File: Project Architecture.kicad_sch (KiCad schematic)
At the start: 4 parts

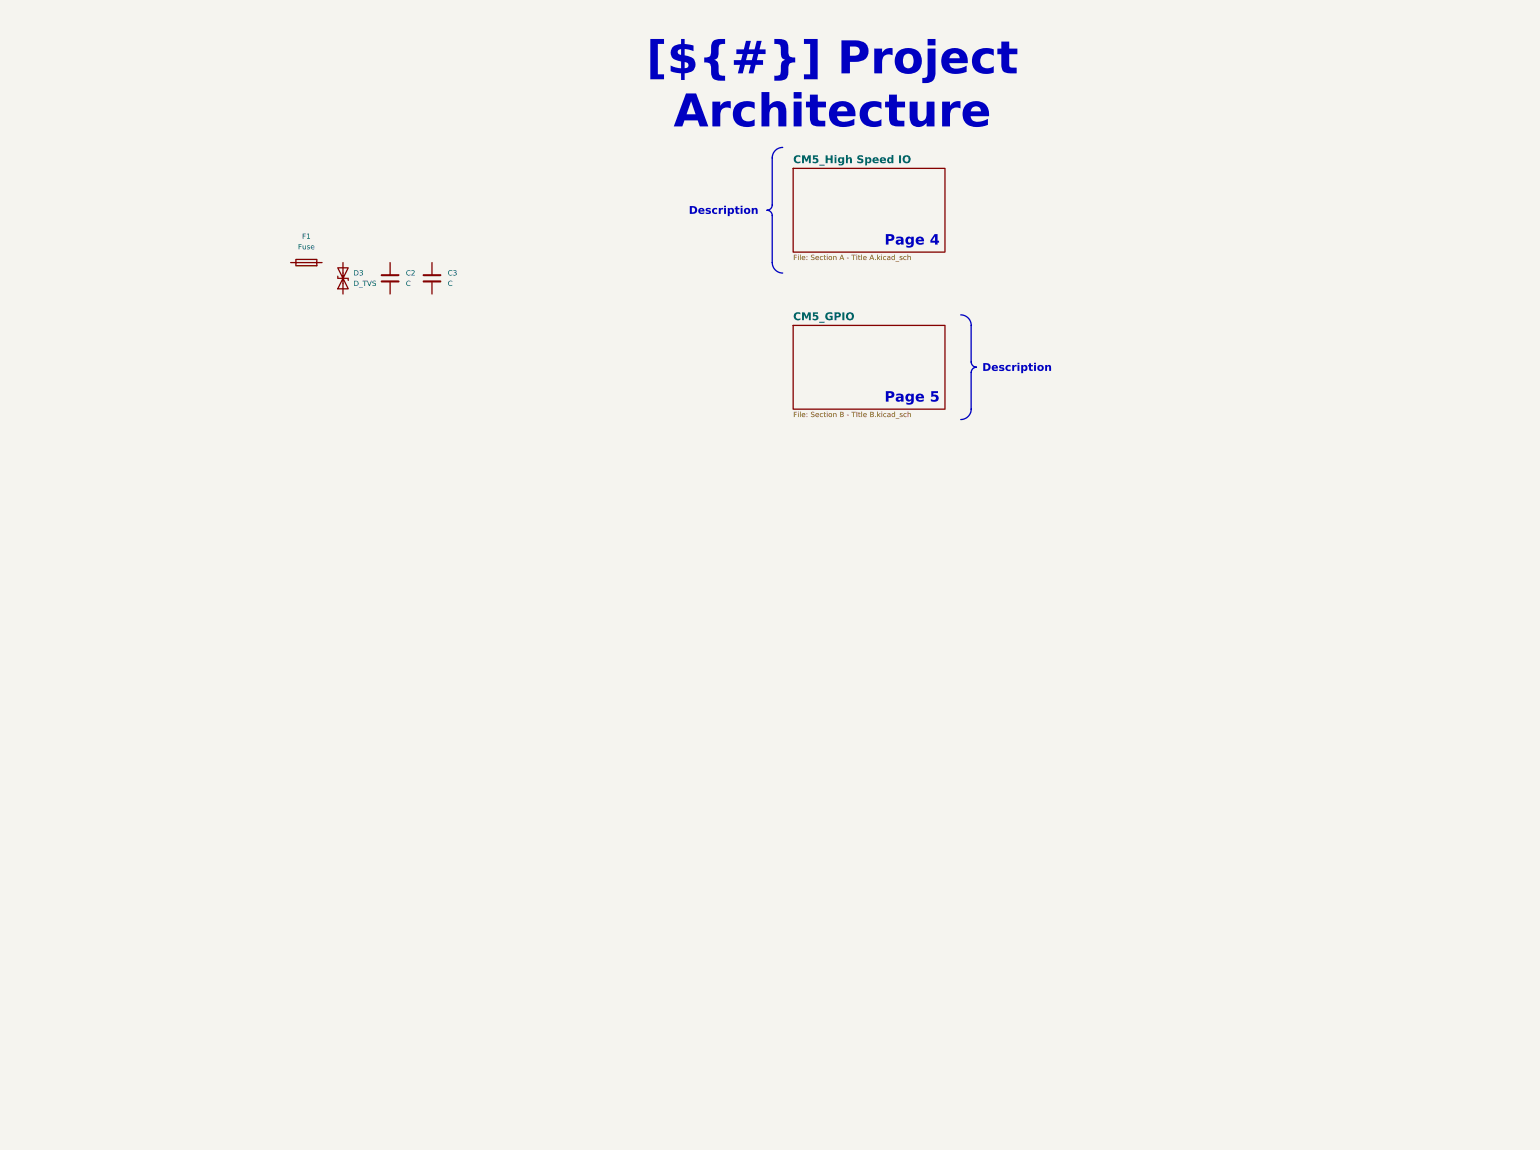
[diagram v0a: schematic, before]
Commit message: Progress in power input and sata power option
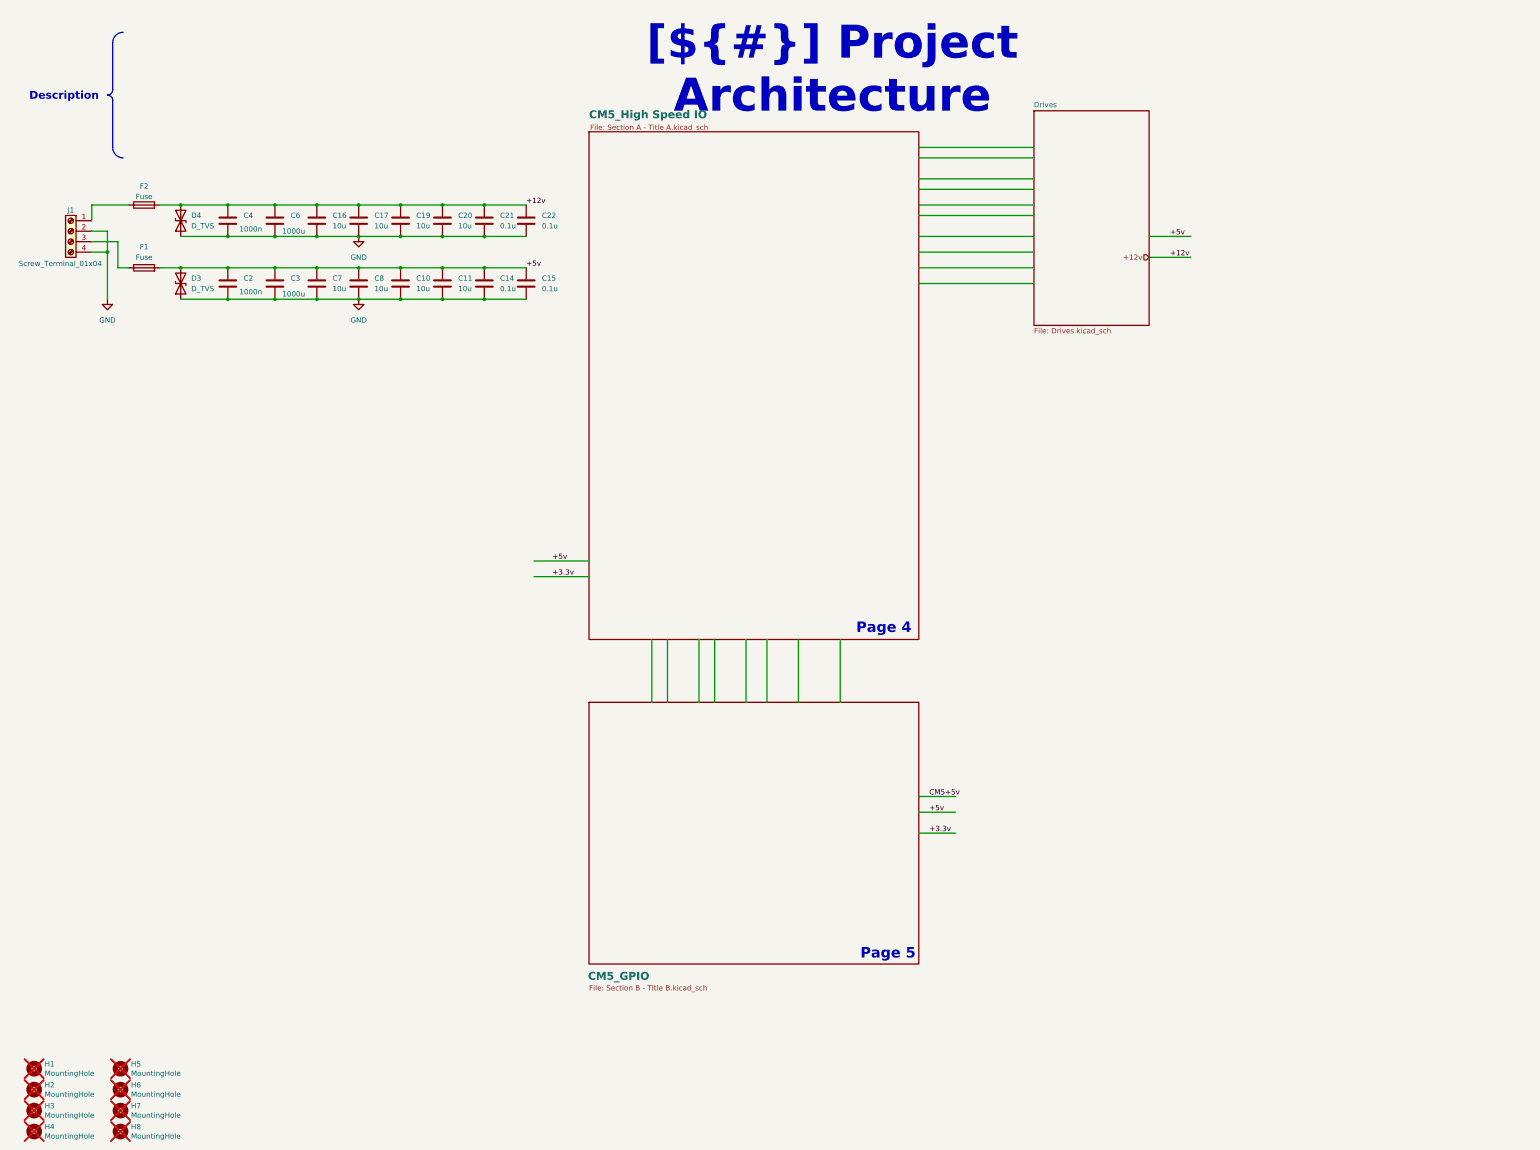
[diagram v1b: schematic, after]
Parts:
- added C10, C11, C16, C17, C19, C20, C7, C8: 10u, symbol Device:C
- added C14, C15, C21, C22: 0.1u, symbol Device:C
- added C4: 1000n, symbol Device:C
- added C6: 1000u, symbol Device:C
- added D4: D_TVS, symbol Device:D_TVS
- added F2: Fuse, symbol Device:Fuse
- added H1, H2, H3, H4, H5, H6, H7, H8: MountingHole, CM5IO:MountingHole_2.7mm_M2.5_DIN965, symbol Mechanical:MountingHole
- added J1: Screw_Terminal_01x04, symbol Connector:Screw_Terminal_01x04
- C2: value C -> 1000n
- C3: value C -> 1000u
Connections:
- net at F1.1: now also J1.3 (Pin_3)
- net +5v: now reaches F1.2
- net +5v: now also C2.1, C3.1, D3.2 (A2), C10.1, C11.1, C14.1, C15.1, C7.1, C8.1
- net GND: now reaches C2.2
- net GND: now also C3.2, D3.1 (A1), C10.2, C11.2, C14.2, C15.2, C16.2, C17.2, C19.2, C20.2, C21.2, C22.2, C4.2, C6.2, C7.2, C8.2, D4.1 (A1), J1.2 (Pin_2), J1.4 (Pin_4)
- new net: F2.1, J1.1 (Pin_1)
- new net +12v: C16.1, C17.1, C19.1, C20.1, C21.1, C22.1, C4.1, C6.1, D4.2 (A2), F2.2
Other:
- added sheet Drives (Drives.kicad_sch)
- moved on the sheet: C2, C3, D3, F1

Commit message: Voltage calcs
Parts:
- renumbered C4 to C1, C20 to C11, C11 to C12, C21 to C13, C22 to C15, C15 to C16, C6 to C3, C3 to C4, C16 to C5, C7 to C6, C17 to C7, C19 to C9, D4 to D1, D3 to D2, F2 to F1, F1 to F2
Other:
- added sheet Sata Drives (Sata_Drives.kicad_sch)
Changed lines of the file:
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@@
 	(wire
 		(pts
+			(xy 231.14 78.74) (xy 259.08 78.74)
+		)
+		(stroke
+			(width 0)
+			(type solid)
+		)
+	)
+	(wire
+		(pts
 			(xy 125.73 63.5) (xy 135.89 63.5)
 		)
@@
 	(wire
 		(pts
+			(xy 231.14 82.55) (xy 259.08 82.55)
+		)
+		(stroke
+			(width 0)
+			(type solid)
+		)
+	)
+	(wire
+		(pts
 			(xy 170.18 161.29) (xy 170.18 176.53)
 		)
@@
 		(on_board yes)
 		(dnp no)
-		(property "Reference" "F2"
+		(property "Reference" "F1"
 			(at 43.18 51.308 90)
 			(effects
@@
 			(project "CM5 Nas"
 				(path "/0650c7a8-acba-429c-9f8e-eec0baf0bc1c/fede4c36-00cc-4d3d-b71c-5243ba232202"
-					(reference "F2")
+					(reference "F1")
 					(unit 1)
 				)
@@
 		(dnp no)
 		(fields_autoplaced yes)
-		(property "Reference" "C22"
+		(property "Reference" "C15"
 			(at 139.7 58.4199 0)
 			(effects
@@
 			(project "CM5 Nas"
 				(path "/0650c7a8-acba-429c-9f8e-eec0baf0bc1c/fede4c36-00cc-4d3d-b71c-5243ba232202"
-					(reference "C22")
+					(reference "C15")
 					(unit 1)
 				)
@@
 		(on_board yes)
 		(dnp no)
-		(property "Reference" "C4"
+		(property "Reference" "C1"
 			(at 67.31 58.4199 0)
 			(effects
@@
 			(project "CM5 Nas"
 				(path "/0650c7a8-acba-429c-9f8e-eec0baf0bc1c/fede4c36-00cc-4d3d-b71c-5243ba232202"
-					(reference "C4")
+					(reference "C1")
 					(unit 1)
 				)
@@
 		(dnp no)
 		(fields_autoplaced yes)
-		(property "Reference" "#PWR03"
+		(property "Reference" "#PWR02"
 			(at 95.25 69.85 0)
 			(effects
@@
 			(project "CM5 Nas"
 				(path "/0650c7a8-acba-429c-9f8e-eec0baf0bc1c/fede4c36-00cc-4d3d-b71c-5243ba232202"
-					(reference "#PWR03")
+					(reference "#PWR02")
 					(unit 1)
 				)
@@
 		(dnp no)
 		(fields_autoplaced yes)
-		(property "Reference" "C16"
+		(property "Reference" "C5"
 			(at 88.9 58.4199 0)
 			(effects
@@
 			(project "CM5 Nas"
 				(path "/0650c7a8-acba-429c-9f8e-eec0baf0bc1c/fede4c36-00cc-4d3d-b71c-5243ba232202"
-					(reference "C16")
+					(reference "C5")
 					(unit 1)
 				)
@@
 		(dnp no)
 		(fields_autoplaced yes)
-		(property "Reference" "C15"
+		(property "Reference" "C16"
 			(at 139.7 73.6599 0)
 			(effects
@@
 			(project "CM5 Nas"
 				(path "/0650c7a8-acba-429c-9f8e-eec0baf0bc1c/fede4c36-00cc-4d3d-b71c-5243ba232202"
-					(reference "C15")
+					(reference "C16")
 					(unit 1)
 				)
@@
 		(dnp no)
 		(fields_autoplaced yes)
-		(property "Reference" "C7"
+		(property "Reference" "C6"
 			(at 88.9 73.6599 0)
 			(effects
@@
 			(project "CM5 Nas"
 				(path "/0650c7a8-acba-429c-9f8e-eec0baf0bc1c/fede4c36-00cc-4d3d-b71c-5243ba232202"
-					(reference "C7")
+					(reference "C6")
 					(unit 1)
 				)
@@
 		(dnp no)
 		(fields_autoplaced yes)
-		(property "Reference" "#PWR01"
+		(property "Reference" "#PWR03"
 			(at 95.25 85.09 0)
 			(effects
@@
 			(project ""
 				(path "/0650c7a8-acba-429c-9f8e-eec0baf0bc1c/fede4c36-00cc-4d3d-b71c-5243ba232202"
-					(reference "#PWR01")
+					(reference "#PWR03")
 					(unit 1)
 				)
@@
 		(dnp no)
 		(fields_autoplaced yes)
-		(property "Reference" "C19"
+		(property "Reference" "C9"
 			(at 109.22 58.4199 0)
 			(effects
@@
 			(project "CM5 Nas"
 				(path "/0650c7a8-acba-429c-9f8e-eec0baf0bc1c/fede4c36-00cc-4d3d-b71c-5243ba232202"
-					(reference "C19")
+					(reference "C9")
 					(unit 1)
 				)
@@
 		(on_board yes)
 		(dnp no)
-		(property "Reference" "F1"
+		(property "Reference" "F2"
 			(at 43.18 66.04 90)
 			(effects
@@
 			(project ""
 				(path "/0650c7a8-acba-429c-9f8e-eec0baf0bc1c/fede4c36-00cc-4d3d-b71c-5243ba232202"
-					(reference "F1")
+					(reference "F2")
 					(unit 1)
 				)
@@
 		(dnp no)
 		(fields_autoplaced yes)
-		(property "Reference" "C11"
+		(property "Reference" "C12"
 			(at 119.38 73.6599 0)
 			(effects
@@
 			(project "CM5 Nas"
 				(path "/0650c7a8-acba-429c-9f8e-eec0baf0bc1c/fede4c36-00cc-4d3d-b71c-5243ba232202"
-					(reference "C11")
+					(reference "C12")
 					(unit 1)
 				)
@@
 		(dnp no)
 		(fields_autoplaced yes)
-		(property "Reference" "C17"
+		(property "Reference" "C7"
 			(at 99.06 58.4199 0)
 			(effects
@@
 			(project "CM5 Nas"
 				(path "/0650c7a8-acba-429c-9f8e-eec0baf0bc1c/fede4c36-00cc-4d3d-b71c-5243ba232202"
-					(reference "C17")
+					(reference "C7")
 					(unit 1)
 				)
@@
 		(dnp no)
 		(fields_autoplaced yes)
-		(property "Reference" "C20"
+		(property "Reference" "C11"
 			(at 119.38 58.4199 0)
 			(effects
@@
 			(project "CM5 Nas"
 				(path "/0650c7a8-acba-429c-9f8e-eec0baf0bc1c/fede4c36-00cc-4d3d-b71c-5243ba232202"
-					(reference "C20")
+					(reference "C11")
 					(unit 1)
 				)
@@
 		(dnp no)
 		(fields_autoplaced yes)
-		(property "Reference" "#PWR02"
+		(property "Reference" "#PWR01"
 			(at 34.29 85.09 0)
 			(effects
@@
 			(project "CM5 Nas"
 				(path "/0650c7a8-acba-429c-9f8e-eec0baf0bc1c/fede4c36-00cc-4d3d-b71c-5243ba232202"
-					(reference "#PWR02")
+					(reference "#PWR01")
 					(unit 1)
 				)
@@
 		(dnp no)
 		(fields_autoplaced yes)
-		(property "Reference" "D4"
+		(property "Reference" "D1"
 			(at 54.61 58.4199 90)
 			(effects
@@
 			(project "CM5 Nas"
 				(path "/0650c7a8-acba-429c-9f8e-eec0baf0bc1c/fede4c36-00cc-4d3d-b71c-5243ba232202"
-					(reference "D4")
+					(reference "D1")
 					(unit 1)
 				)
@@
 		(on_board yes)
 		(dnp no)
-		(property "Reference" "C6"
+		(property "Reference" "C3"
 			(at 78.74 58.4199 0)
 			(effects
@@
 			(project "CM5 Nas"
 				(path "/0650c7a8-acba-429c-9f8e-eec0baf0bc1c/fede4c36-00cc-4d3d-b71c-5243ba232202"
-					(reference "C6")
+					(reference "C3")
 					(unit 1)
 				)
@@
 		(dnp no)
 		(fields_autoplaced yes)
-		(property "Reference" "C21"
+		(property "Reference" "C13"
 			(at 129.54 58.4199 0)
 			(effects
@@
 			(project "CM5 Nas"
 				(path "/0650c7a8-acba-429c-9f8e-eec0baf0bc1c/fede4c36-00cc-4d3d-b71c-5243ba232202"
-					(reference "C21")
+					(reference "C13")
 					(unit 1)
 				)
@@
 		(dnp no)
 		(fields_autoplaced yes)
-		(property "Reference" "D3"
+		(property "Reference" "D2"
 			(at 54.61 73.6599 90)
 			(effects
@@
 			(project ""
 				(path "/0650c7a8-acba-429c-9f8e-eec0baf0bc1c/fede4c36-00cc-4d3d-b71c-5243ba232202"
-					(reference "D3")
+					(reference "D2")
 					(unit 1)
 				)
@@
 		(on_board yes)
 		(dnp no)
-		(property "Reference" "C3"
+		(property "Reference" "C4"
 			(at 78.74 73.6599 0)
 			(effects
@@
 			(project "CM5 Nas"
 				(path "/0650c7a8-acba-429c-9f8e-eec0baf0bc1c/fede4c36-00cc-4d3d-b71c-5243ba232202"
-					(reference "C3")
+					(reference "C4")
 					(unit 1)
 				)
@@
 				)
 			)
+		)
+	)
+	(sheet
+		(at 259.08 92.71)
+		(size 27.94 68.58)
+		(exclude_from_sim no)
+		(in_bom yes)
+		(on_board yes)
+		(dnp no)
+		(fields_autoplaced yes)
+		(stroke
+			(width 0.1524)
+			(type solid)
+		)
+		(fill
+			(color 0 0 0 0.0000)
+		)
+		(property "Sheetname" "Sata Drives"
+			(at 259.08 91.9984 0)
+			(effects
+				(font
+					(size 1.27 1.27)
+				)
+				(justify left bottom)
+			)
+		)
+		(property "Sheetfile" "Sata_Drives.kicad_sch"
+			(at 259.08 161.8746 0)
+			(effects
+				(font
+					(size 1.27 1.27)
+				)
+				(justify left top)
+			)
+		)
+		(instances
+			(project "CM5 Nas"
+				(path "/0650c7a8-acba-429c-9f8e-eec0baf0bc1c/fede4c36-00cc-4d3d-b71c-5243ba232202"
+					(page "8")
+				)
+			)
